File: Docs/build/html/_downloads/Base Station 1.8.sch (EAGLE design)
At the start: 21 parts, among them IC1 FT230XS, J1 POWER_JACKPTH, Q1 2222A, U2 TINY85-20-DIP

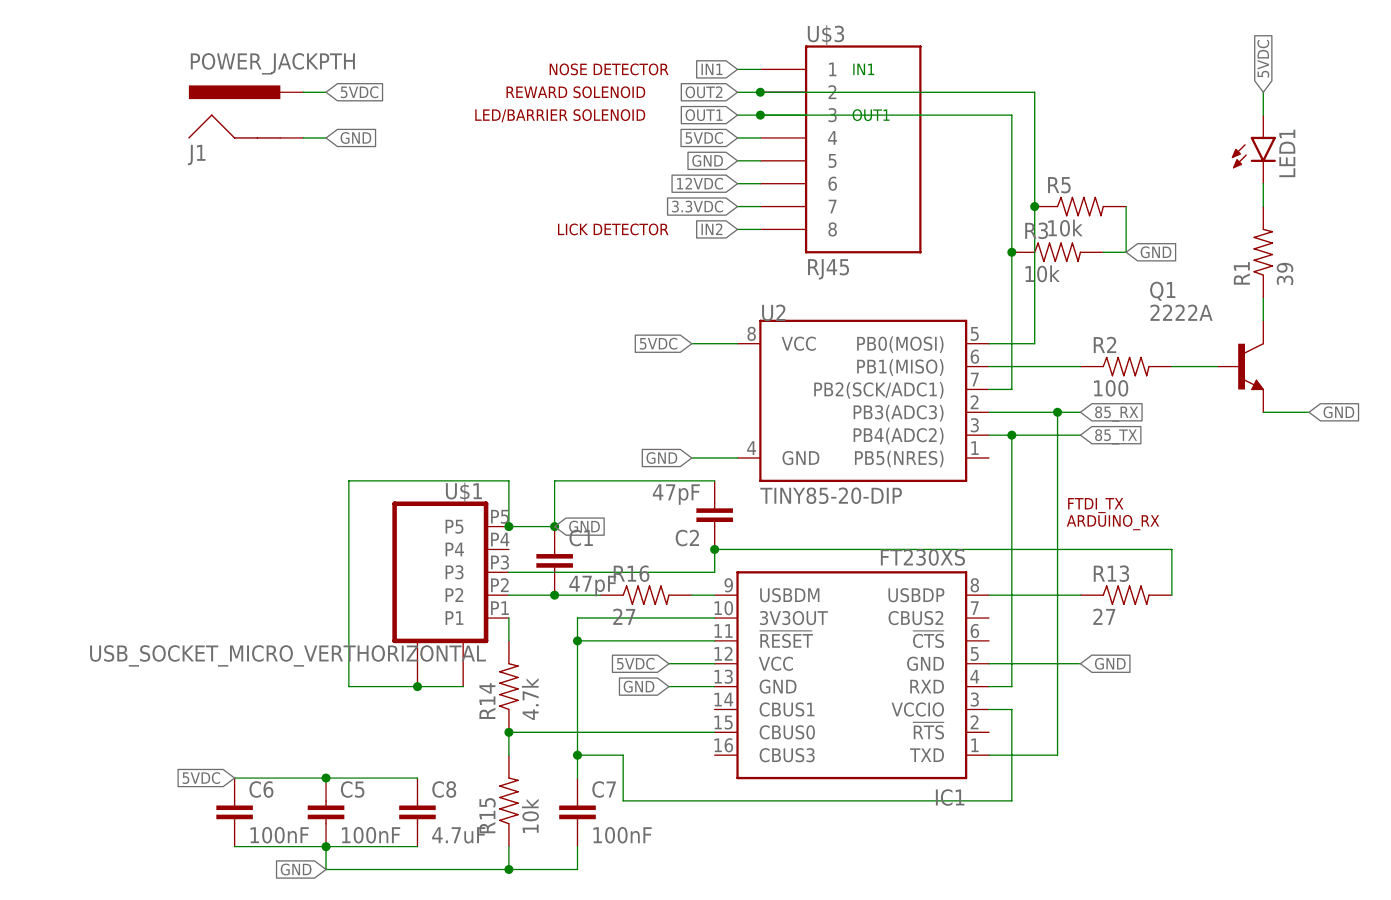
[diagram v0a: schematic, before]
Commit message: Base station PCB update: Changed to reinforced micro usb for more solid connection. Made 47 pF labels visible. Added OSH logo moved FTDI chip to bottom for easier soldering of the chip and the micro usb Added breakouts for input 1 and input 2.
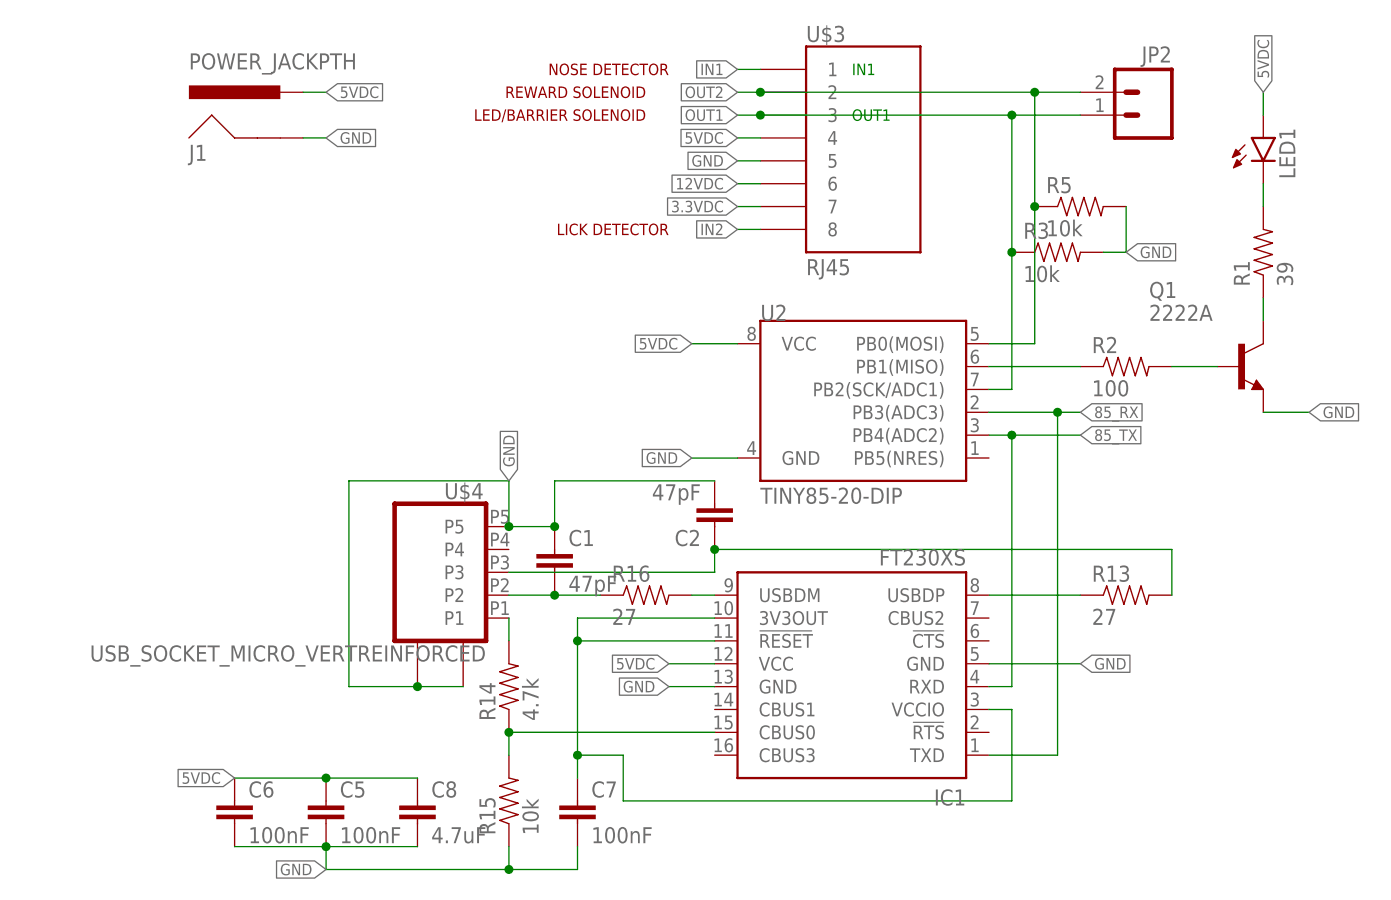
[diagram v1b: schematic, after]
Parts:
- removed U$1: USB_SOCKET_MICRO_VERTHORIZONTAL, Andy-library:USB_SOCKET_MICRO_VERTHORIZONTAL
- added JP2: (no value), SparkFun-Connectors:M021X02_NO_SILK
- added U$4: USB_SOCKET_MICRO_VERTREINFORCED, Andy-library:USB_SOCKET_MICRO_VERTREINFORCED
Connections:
- net GND: now also U$4.P$1, U$4.P$2, U$4.P5; no longer U$1.P$1, U$1.P$2, U$1.P5
- net N$10: now also U$4.P3; no longer U$1.P3
- net N$12: now also U$4.P1; no longer U$1.P1
- net N$9: now also U$4.P2; no longer U$1.P2
- net OUT1: now also JP2.1
- net OUT2: now also JP2.2
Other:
- note removed: "FTDI_TX ARDUINO_RX"
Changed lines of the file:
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@@
 <?xml version="1.0" encoding="utf-8"?>
 <!DOCTYPE eagle SYSTEM "eagle.dtd">
-<eagle version="7.3.0">
+<eagle version="7.6.0">
 <drawing>
 <settings>
@@
 <layer number="112" name="tSilk" color="7" fill="1" visible="yes" active="yes"/>
 <layer number="113" name="IDFDebug" color="7" fill="1" visible="yes" active="yes"/>
-<layer number="114" name="Badge_Outline" color="11" fill="1" visible="no" active="no"/>
+<layer number="114" name="Badge_Outline" color="7" fill="1" visible="yes" active="yes"/>
+<layer number="115" name="ReferenceISLANDS" color="7" fill="1" visible="yes" active="yes"/>
 <layer number="116" name="Patch_BOT" color="9" fill="4" visible="yes" active="yes"/>
 <layer number="118" name="Rect_Pads" color="7" fill="1" visible="yes" active="yes"/>
@@
 <part name="IC1" library="ftdichip" deviceset="FT230X" device="S"/>
 <part name="LED1" library="Andy-library" deviceset="LED" device=""/>
-<part name="U$1" library="Andy-library" deviceset="USB_SOCKET_MICRO_VERT" device="HORIZONTAL"/>
 <part name="R2" library="SparkFun-Resistors" deviceset="RESISTOR" device="PTH-1/4W-VERT" value="100"/>
 <part name="R3" library="SparkFun-Resistors" deviceset="RESISTOR" device="PTH-1/4W-VERT" value="10k"/>
@@
 <part name="C2" library="SparkFun-Capacitors" deviceset="CAP" device="PTH" value="47pF"/>
 <part name="J1" library="Andy-library" deviceset="POWER_JACK" device="PTH"/>
-<part name="FRAME1" library="frames" deviceset="A5L-LOC" device=""/>
+<part name="U$4" library="Andy-library" deviceset="USB_SOCKET_MICRO_VERT" device="REINFORCED"/>
+<part name="JP2" library="SparkFun-Connectors" deviceset="M02" device="1X02_NO_SILK"/>
+<part name="FRAME1" library="frames" deviceset="A5L-LOC" device="" value="For more information see \n http://cerebro.readthedocs.io/"/>
 </parts>
 <sheets>
@@
 <text x="17.78" y="40.64" size="1.27" layer="91" align="center-left">OUT1</text>
 <text x="17.78" y="45.72" size="1.27" layer="91" align="center-left">IN1</text>
-<text x="41.656" y="-5.08" size="1.27" layer="94">FTDI_TX
-ARDUINO_RX</text>
 </plain>
 <instances>
@@
 <instance part="IC1" gate="G$1" x="17.78" y="-22.86" rot="R180"/>
 <instance part="LED1" gate="G$1" x="63.5" y="38.1"/>
-<instance part="U$1" gate="G$1" x="-27.94" y="-10.16" rot="MR0"/>
 <instance part="R2" gate="G$1" x="48.26" y="12.7"/>
 <instance part="R3" gate="G$1" x="40.64" y="25.4"/>
@@
 <instance part="C2" gate="G$1" x="2.54" y="-2.54" rot="R180"/>
 <instance part="J1" gate="G$1" x="-45.72" y="35.56"/>
-<instance part="FRAME1" gate="G$1" x="-83.82" y="-68.58"/>
+<instance part="U$4" gate="G$1" x="-27.94" y="-10.16" rot="MR0"/>
+<instance part="JP2" gate="G$1" x="50.8" y="40.64" rot="MR0"/>
+<instance part="FRAME1" gate="G$1" x="-83.82" y="-63.5"/>
 </instances>
 <busses>
@@
 <segment>
 <wire x1="-20.32" y1="-5.08" x2="-15.24" y2="-5.08" width="0.1524" layer="91"/>
-<label x="-15.24" y="-5.08" size="1.27" layer="95" xref="yes"/>
 <wire x1="-20.32" y1="-5.08" x2="-20.32" y2="0" width="0.1524" layer="91"/>
 <junction x="-20.32" y="-5.08"/>
 <wire x1="-38.1" y1="0" x2="-20.32" y2="0" width="0.1524" layer="91"/>
 <wire x1="-38.1" y1="0" x2="-38.1" y2="-22.86" width="0.1524" layer="91"/>
-<pinref part="U$1" gate="G$1" pin="P5"/>
-<pinref part="U$1" gate="G$1" pin="P$2"/>
-<pinref part="U$1" gate="G$1" pin="P$1"/>
 <wire x1="-25.4" y1="-22.86" x2="-30.48" y2="-22.86" width="0.1524" layer="91"/>
 <wire x1="-30.48" y1="-22.86" x2="-38.1" y2="-22.86" width="0.1524" layer="91"/>
@@
 <wire x1="-15.24" y1="0" x2="-15.24" y2="-5.08" width="0.1524" layer="91"/>
 <junction x="-15.24" y="-5.08"/>
+<pinref part="U$4" gate="G$1" pin="P5"/>
+<pinref part="U$4" gate="G$1" pin="P$1"/>
+<pinref part="U$4" gate="G$1" pin="P$2"/>
+<label x="-20.32" y="0" size="1.27" layer="95" rot="R90" xref="yes"/>
 </segment>
 <segment>
@@
 <wire x1="7.62" y1="43.18" x2="38.1" y2="43.18" width="0.1524" layer="91"/>
 <junction x="7.62" y="43.18"/>
+<pinref part="JP2" gate="G$1" pin="2"/>
+<wire x1="43.18" y1="43.18" x2="38.1" y2="43.18" width="0.1524" layer="91"/>
+<junction x="38.1" y="43.18"/>
 </segment>
 </net>
@@
 <pinref part="R3" gate="G$1" pin="1"/>
 <junction x="35.56" y="25.4"/>
+<pinref part="JP2" gate="G$1" pin="1"/>
+<wire x1="43.18" y1="40.64" x2="35.56" y2="40.64" width="0.1524" layer="91"/>
+<junction x="35.56" y="40.64"/>
 </segment>
 </net>
@@
 <segment>
 <wire x1="-20.32" y1="-15.24" x2="-20.32" y2="-17.78" width="0.1524" layer="91"/>
-<pinref part="U$1" gate="G$1" pin="P1"/>
 <pinref part="R14" gate="G$1" pin="2"/>
+<pinref part="U$4" gate="G$1" pin="P1"/>
 </segment>
 </net>
@@
 <segment>
 <wire x1="-20.32" y1="-12.7" x2="-15.24" y2="-12.7" width="0.1524" layer="91"/>
-<pinref part="U$1" gate="G$1" pin="P2"/>
 <pinref part="R16" gate="G$1" pin="1"/>
 <pinref part="C1" gate="G$1" pin="2"/>
 <wire x1="-15.24" y1="-12.7" x2="-10.16" y2="-12.7" width="0.1524" layer="91"/>
 <junction x="-15.24" y="-12.7"/>
+<pinref part="U$4" gate="G$1" pin="P2"/>
 </segment>
 </net>
@@
 <wire x1="2.54" y1="-7.62" x2="53.34" y2="-7.62" width="0.1524" layer="91"/>
 <wire x1="53.34" y1="-7.62" x2="53.34" y2="-12.7" width="0.1524" layer="91"/>
-<pinref part="U$1" gate="G$1" pin="P3"/>
 <pinref part="R13" gate="G$1" pin="2"/>
 <pinref part="C2" gate="G$1" pin="1"/>
 <junction x="2.54" y="-7.62"/>
-</segment>
-</net>
+<pinref part="U$4" gate="G$1" pin="P3"/>
+</segment>
+</net>
